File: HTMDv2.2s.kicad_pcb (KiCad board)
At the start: 2 copper layers, 90 x 49.9 mm, 120 parts, among them IC1 TJA1441AT_0Z, IC2 A3921KLPTR-T, IC3 TMP275AQDGKRQ1, J1 Conn_01x04, J10 Conn_01x02, J11 Conn_01x02, J2 Conn_01x04, J3 Conn_01x06, J4 Conn_01x01, J5 Conn_01x01_Pin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

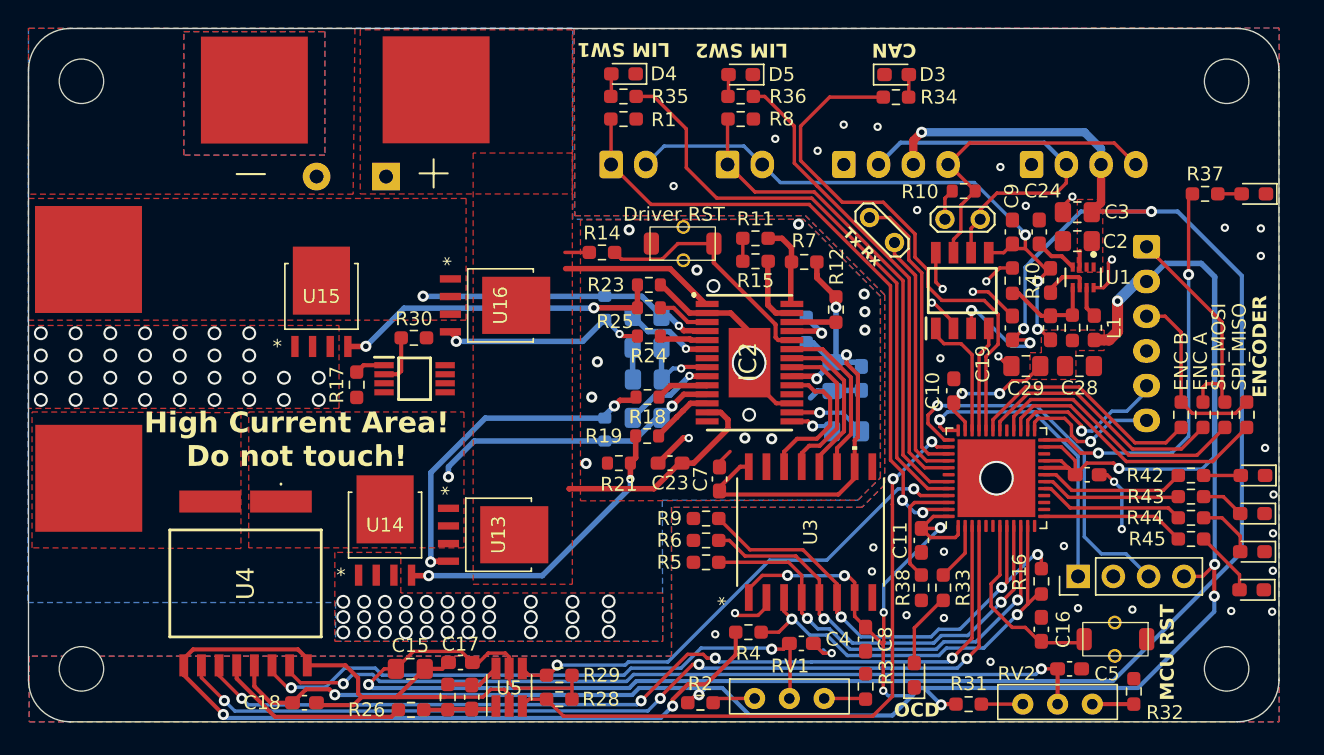
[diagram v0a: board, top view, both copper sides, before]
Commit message: update
温度センサ周りの配線
プルダウン抵抗の位置変更
ドライブラインのLED追加
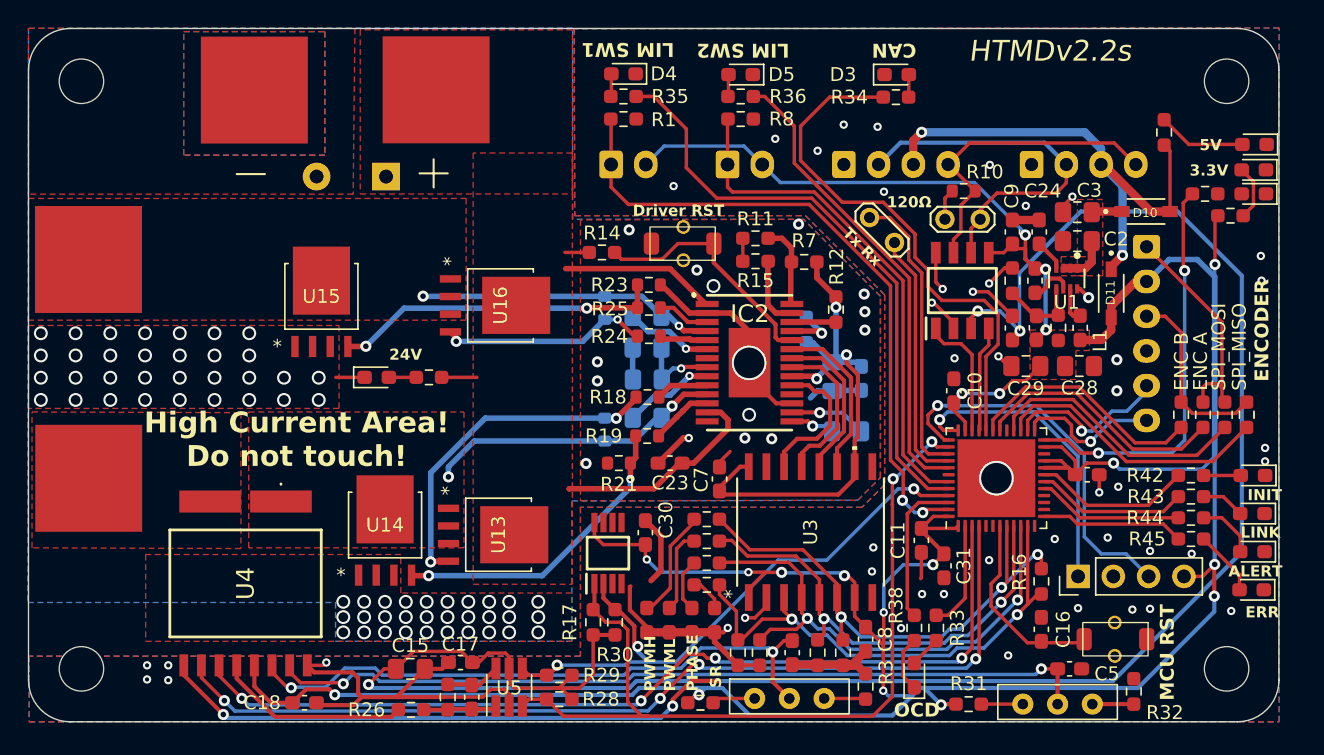
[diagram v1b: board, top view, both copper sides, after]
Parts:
- added C30: 0.1u, Capacitor_SMD:C_0603_1608Metric_Pad1.08x0.95mm_HandSolder, F.Cu at (107.9, 75.3)
- added C31: 1u, Capacitor_SMD:C_0603_1608Metric_Pad1.08x0.95mm_HandSolder, F.Cu at (129.4, 77.7)
- added D10: D, 0-Myparts:SS2040FL, F.Cu at (143.9, 52.2)
- added D11: D, 0-Myparts:SS2040FL, F.Cu at (141.4, 58.1)
- added D12: LED, LED_SMD:LED_0603_1608Metric_Pad1.05x0.95mm_HandSolder, F.Cu at (151.7, 49.2)
- added D13: LED, LED_SMD:LED_0603_1608Metric_Pad1.05x0.95mm_HandSolder, F.Cu at (151.7, 47.3)
- added D14: LED, LED_SMD:LED_0603_1608Metric_Pad1.05x0.95mm_HandSolder, F.Cu at (88.6, 64.1)
- added D15: LED, LED_SMD:LED_0603_1608Metric_Pad1.05x0.95mm_HandSolder, F.Cu at (108.0, 81.6)
- added D16: LED, LED_SMD:LED_0603_1608Metric_Pad1.05x0.95mm_HandSolder, F.Cu at (109.6, 81.6)
- added D17: LED, LED_SMD:LED_0603_1608Metric_Pad1.05x0.95mm_HandSolder, F.Cu at (111.3, 81.6)
- added D18: LED, LED_SMD:LED_0603_1608Metric_Pad1.05x0.95mm_HandSolder, F.Cu at (112.9, 81.6)
- added R46: R, Resistor_SMD:R_0603_1608Metric_Pad0.98x0.95mm_HandSolder, F.Cu at (150.0, 52.5)
- added R47: R, Resistor_SMD:R_0603_1608Metric_Pad0.98x0.95mm_HandSolder, F.Cu at (145.2, 46.5)
- added R48: R, Resistor_SMD:R_0603_1608Metric_Pad0.98x0.95mm_HandSolder, F.Cu at (92.3, 64.1)
- added R49: R, Resistor_SMD:R_0603_1608Metric_Pad0.98x0.95mm_HandSolder, F.Cu at (112.3, 74.3)
- added R50: R, Resistor_SMD:R_0603_1608Metric_Pad0.98x0.95mm_HandSolder, F.Cu at (112.3, 75.9)
- added R51: R, Resistor_SMD:R_0603_1608Metric_Pad0.98x0.95mm_HandSolder, F.Cu at (112.3, 77.5)
- added R52: R, Resistor_SMD:R_0603_1608Metric_Pad0.98x0.95mm_HandSolder, F.Cu at (112.3, 79.0)
- U13, U14, U15: value PowerPAK_SO-8L_3_VIS -> SQJ180EP-T1_GE3
- moved R30 25.1 mm to (105.7, 81.7), turned to 90 degrees
- moved R17 24.1 mm to (104.1, 81.7)
- moved IC3 18.7 mm to (105.2, 76.8), turned to 90 degrees
- moved R9 13.8 mm to (122.1, 83.9), turned to 90 degrees
- moved R6 11.4 mm to (120.3, 83.9), turned to 90 degrees
- moved R5 7.56 mm to (116.1, 83.9), turned to 90 degrees
- moved R33 2.94 mm to (128.8, 82.1)
- moved R38 2.94 mm to (127.3, 82.1)
- moved R4 1.66 mm to (114.6, 83.9), turned to 90 degrees
- moved U1 1.18 mm to (138.2, 57.0)
- moved R41 1.12 mm to (135.9, 57.1)
- moved C25 1.02 mm to (136.0, 60.5)
- moved L1 1.02 mm to (139.2, 60.5)
- moved R39 1.02 mm to (137.6, 60.5)
- moved C4 0.94 mm to (118.5, 83.9), turned to -90 degrees
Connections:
- C2 pad 1: VCC -> Net-(D10-K)
- C3 pad 1: VCC -> Net-(D10-K)
- U1 pad 1: VCC -> Net-(D10-K)
- U1 pad 2: VCC -> Net-(D10-K)
- U1 pad 3: VCC -> Net-(D10-K)
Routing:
- net +3.3V: track 232.0 -> 251.7 mm, vias 17 -> 19
- net VCC: track 166.2 -> 181.5 mm, vias 6 -> 5
- net GND: track 110.1 -> 123.6 mm, vias 42 -> 49
- net I2C_SCL: track 51.0 -> 60.9 mm
- net Net-(D15-A): track 0.00 -> 7.96 mm
- net Net-(D10-K): track 0.00 -> 6.78 mm
- net OPHASE1: track 30.9 -> 37.3 mm
- net Net-(D13-A): track 0.00 -> 6.36 mm
- net Net-(D16-A): track 0.00 -> 5.97 mm
- net OSR1: track 32.6 -> 36.6 mm
- net Net-(D12-A): track 0.00 -> 3.96 mm
- net Net-(D17-A): track 0.00 -> 3.85 mm
- net LED_OCD: track 4.18 -> 7.79 mm
- net I2C_SDA: track 40.4 -> 43.8 mm, vias 2 -> 3
- net Net-(D2-A): track 5.43 -> 2.27 mm
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- added copper zone on F.Cu, net Net-(D10-K)
- removed copper zone on F.Cu, net VCC
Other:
- board text added: "120Ω"
- board text added: "24V"
- board text added: "3.3V"
- board text added: "5V"
- board text added: "ALERT"
- board text added: "ERR"
- board text added: "HTMDv2.2s"
- board text added: "INIT"
- board text added: "LINK"
- board text added: "PHASE"
- board text added: "PWMH"
- board text added: "PWML"
- board text added: "SR"

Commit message: Update HTMDv2.2s.kicad_pcb
配線の微調整
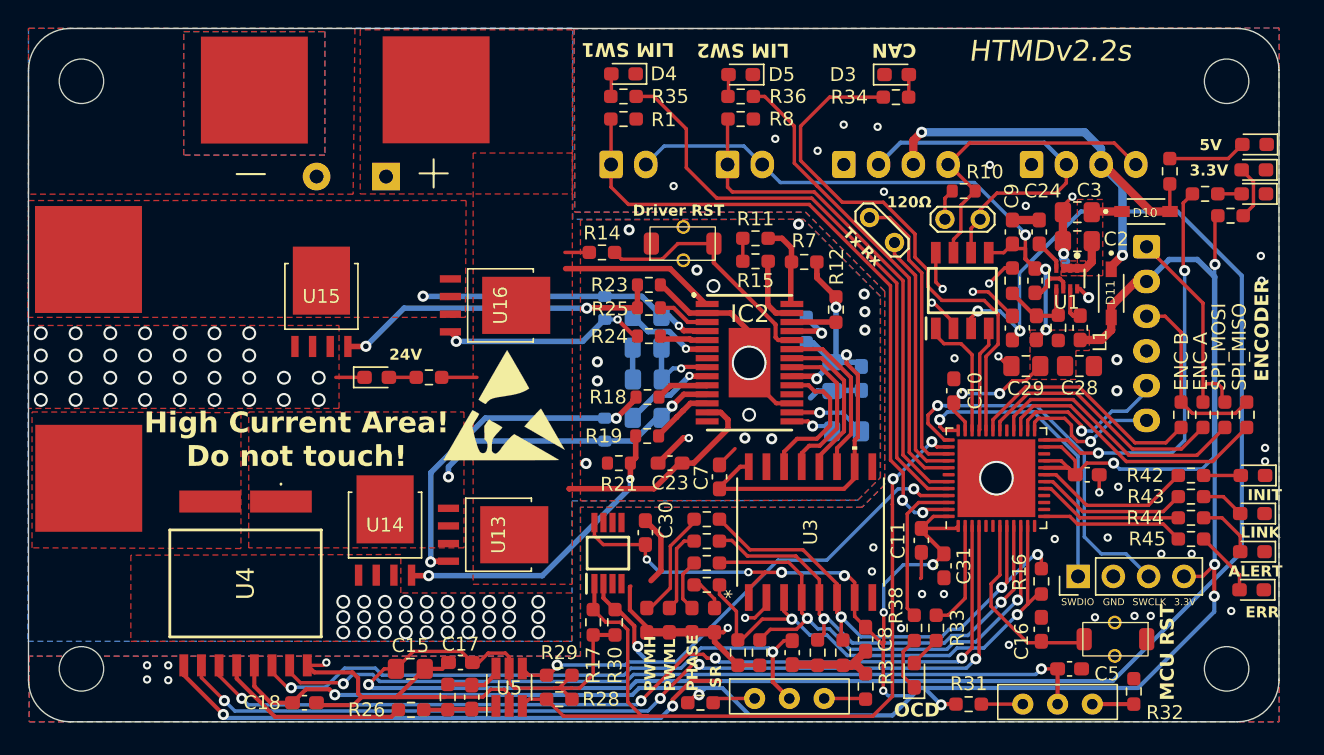
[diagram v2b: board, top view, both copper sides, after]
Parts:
- added REF**: ESD-Logo_8.9x8mm_SilkScreen, Symbol:ESD-Logo_8.9x8mm_SilkScreen, F.Cu at (97.7, 66.1)
- moved R47 2.82 mm to (145.6, 49.3)
- moved C7 0.15 mm to (113.2, 71.3)
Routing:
- net GND: track 123.6 -> 127.3 mm
- net VCC: track 181.5 -> 178.5 mm
- net Net-(D6-A): track 0.00 -> 1.72 mm
- net Net-(D13-A): track 6.36 -> 5.64 mm
- net Net-(J3-Pin_1): track 16.2 -> 15.6 mm
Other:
- board text added: "GND"
- board text added: "SWCLK"
- board text added: "SWDIO"

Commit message: Update HTMDv2.2s.kicad_pcb
ねじ端子直下にビアを追加
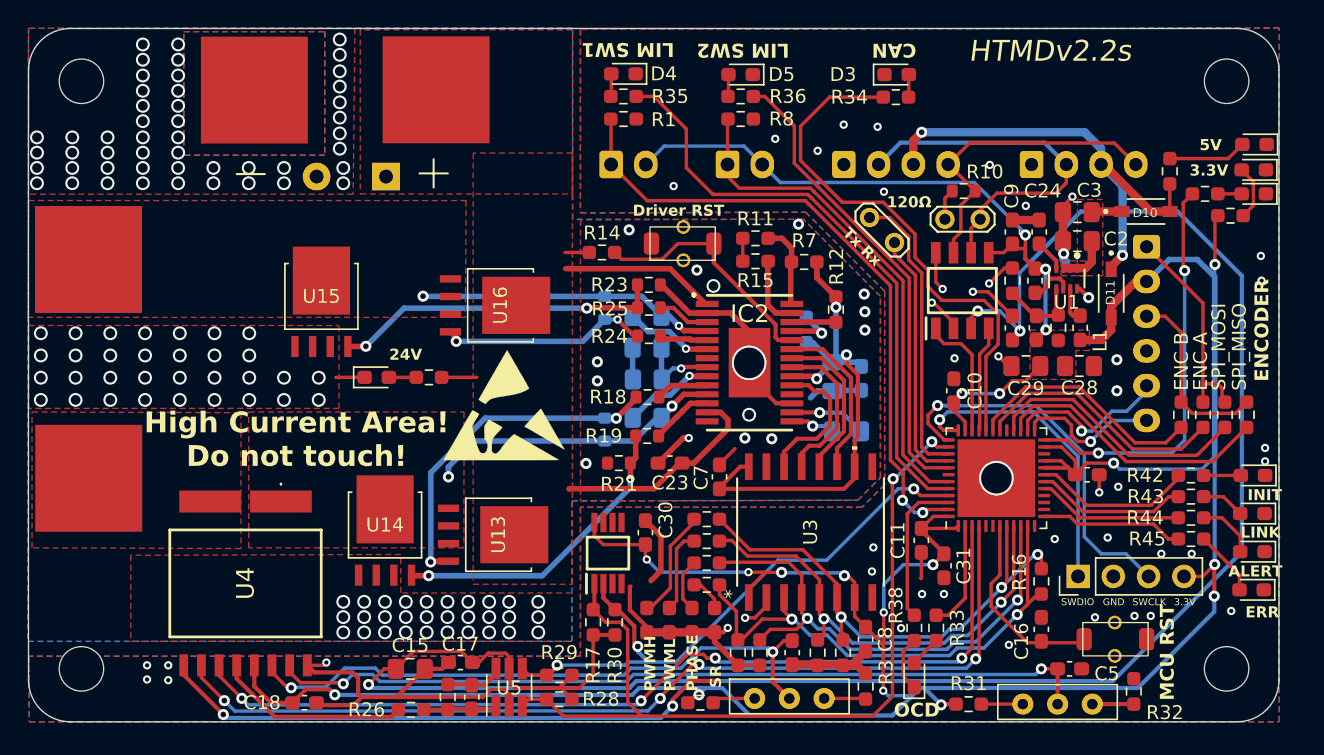
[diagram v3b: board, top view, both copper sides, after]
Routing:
- net LIM1: track 47.6 -> 46.6 mm
- net GNDPWR: vias 77 -> 125

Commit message: update
ティアドロップの追加
DRCの解消
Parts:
- moved C4 0.25 mm to (118.2, 83.9)
- moved D13 0.16 mm to (151.7, 47.2)
- moved D12 0.10 mm to (151.7, 49.1)
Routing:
- net GND: track 127.3 -> 129.8 mm, vias 49 -> 74
- net GNDPWR: track 30.6 -> 30.4 mm, vias 125 -> 131
